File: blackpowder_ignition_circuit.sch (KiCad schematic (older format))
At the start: 11 parts, among them J2 Conn_01x02, J3 Conn_01x02, Q1 FDS6898A, Q2 Q_DUAL_PMOS_S1G1D2S2G2D1, U2 TC4427AVOA

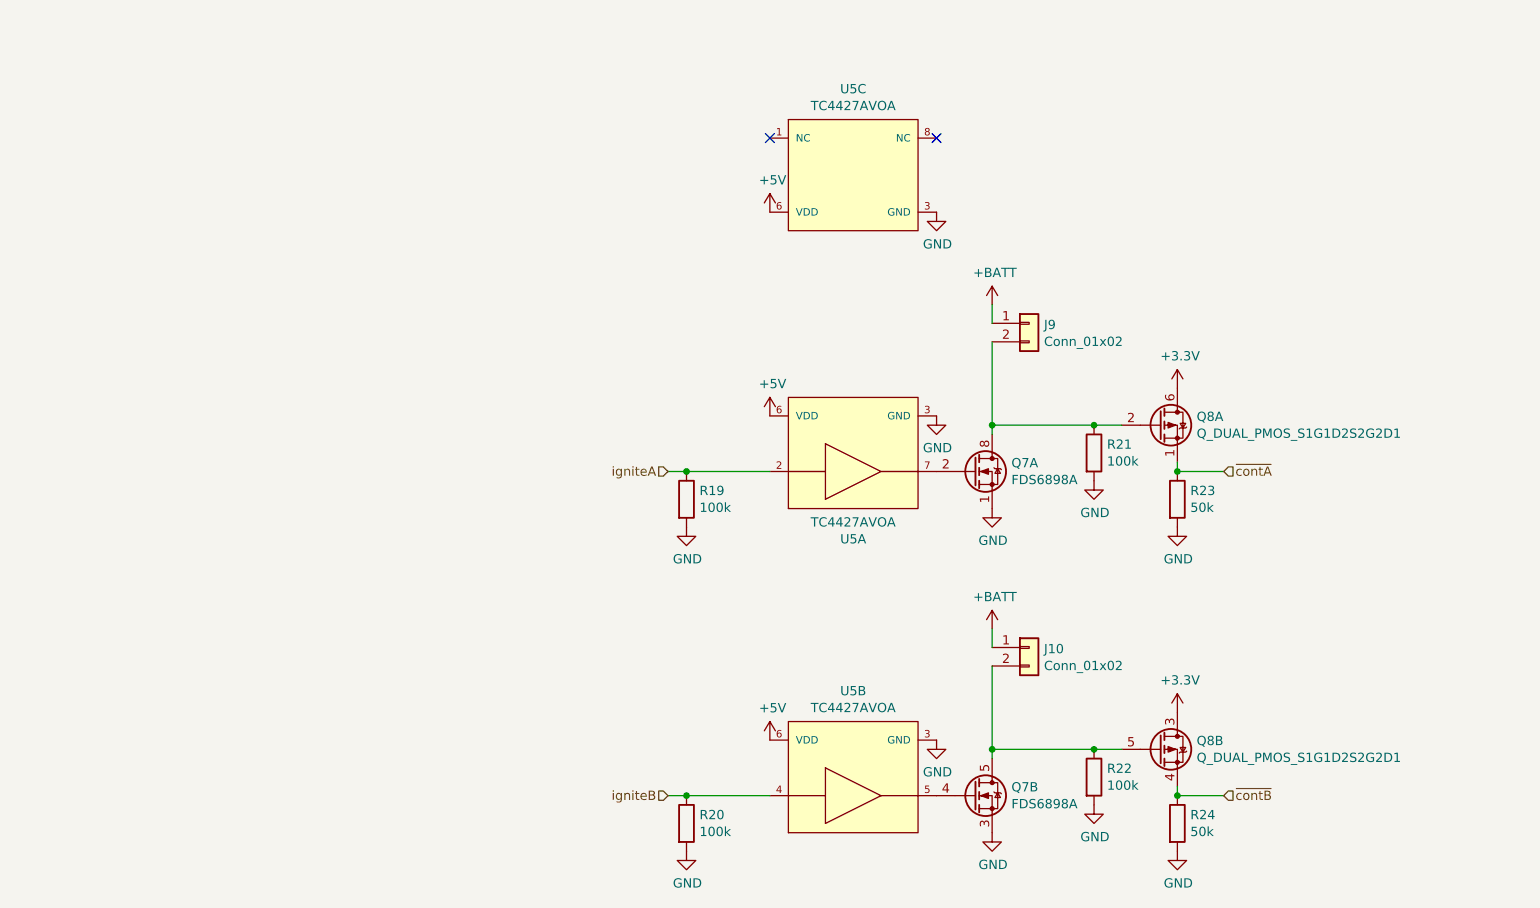
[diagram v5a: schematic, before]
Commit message: added digikey and manf part numbers, BAC logo
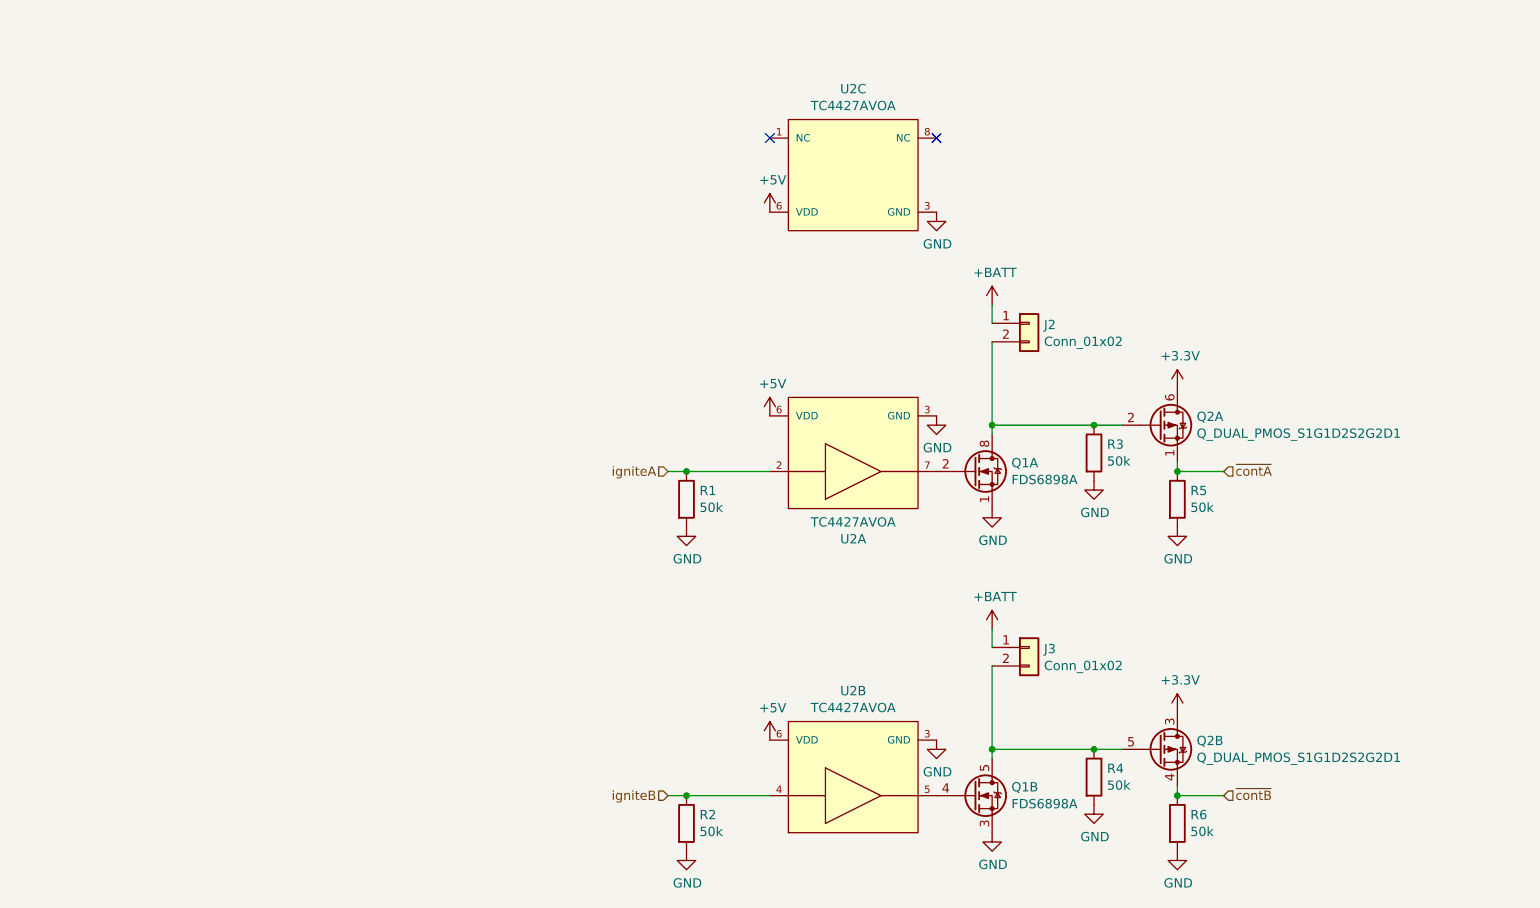
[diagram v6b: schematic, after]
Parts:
- removed R4: 50k, Resistor_SMD:R_0603_1608Metric_Pad0.98x0.95mm_HandSolder, symbol Device:R
- removed R4: 100k, Resistor_SMD:R_0603_1608Metric_Pad0.98x0.95mm_HandSolder, symbol Device:R
- added R4, R5: 50k, Resistor_SMD:R_0603_1608Metric_Pad0.98x0.95mm_HandSolder, symbol Device:R
- J2, J3: DIGIKEY (none) -> WM16206-ND; MANF (none) -> 1724480002
- Q1: DIGIKEY (none) -> FDS6898ACT-ND; MANF (none) -> FDS6898A
- Q2: DIGIKEY (none) -> 742-SI1967DH-T1-BE3CT-ND; MANF (none) -> SI1967DH-T1-BE3
- R1, R2, R3: value 100k -> 50k; DIGIKEY (none) -> 311-51KGRCT-ND; MANF (none) -> RC0603JR-0751KL
- R6: DIGIKEY (none) -> 311-51KGRCT-ND; MANF (none) -> RC0603JR-0751KL
- U2: DIGIKEY (none) -> TC4427AVOA-ND; MANF (none) -> TC4427AVOA
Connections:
- net GND: now also R4.2, R5.2
- net ~contA~: now also R5.1
- net at J3.2 (Pin_2), Q1.5 (D2), Q1.6 (D2)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: now also R4.1

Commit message: updates based on review
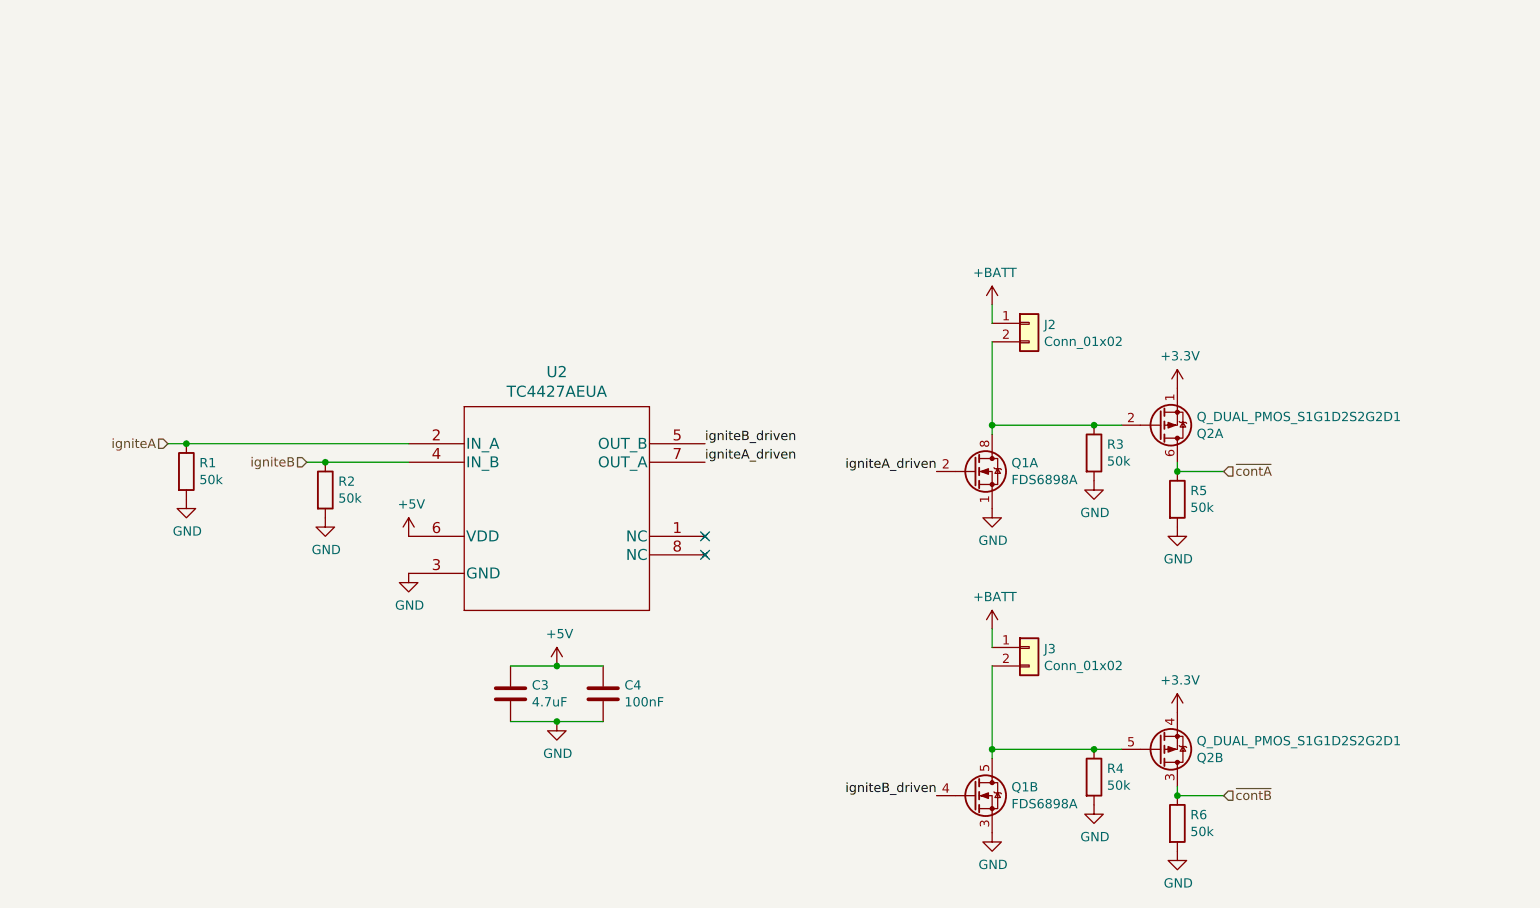
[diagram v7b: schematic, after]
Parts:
- removed U2: TC4427AVOA, Package_SO:MSOP-8-1EP_3x3mm_P0.65mm_EP2.5x3mm_Mask1.73x2.36mm, symbol eec:TC4427AVOA
- added C5: 4.7uF, Capacitor_SMD:C_0603_1608Metric_Pad1.08x0.95mm_HandSolder, symbol Device:C
- added C6: 100nF, Capacitor_SMD:C_0603_1608Metric_Pad1.08x0.95mm_HandSolder, symbol Device:C
- added U2: TC4427AEUA, star-common-lib:TC4427AEUA, symbol star-common-lib:TC4427AEUA
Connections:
- net +3V3: now also Q2.1 (S), Q2.4 (S); no longer Q2.3 (D), Q2.6 (D)
- net +5V: now also C5.1, C6.1, U2.6 (VDD)
- net GND: now also C5.2, C6.2, U2.3 (GND)
- net igniteA: now also U2.2 (IN_A)
- net igniteB: now also U2.4 (IN_B)
- net ~contA~: now also Q2.6 (D); no longer Q2.1 (S)
- net ~contB~: now also Q2.3 (D); no longer Q2.4 (S)
- net igniteA_driven: now reaches Q1.2 (G1)
- net igniteA_driven: now also U2.7 (OUT_A)
- net igniteB_driven: now reaches Q1.4 (G2)
- net igniteB_driven: now also U2.5 (OUT_B)
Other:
- moved on the sheet: R1, R2

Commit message: added diodes for esd
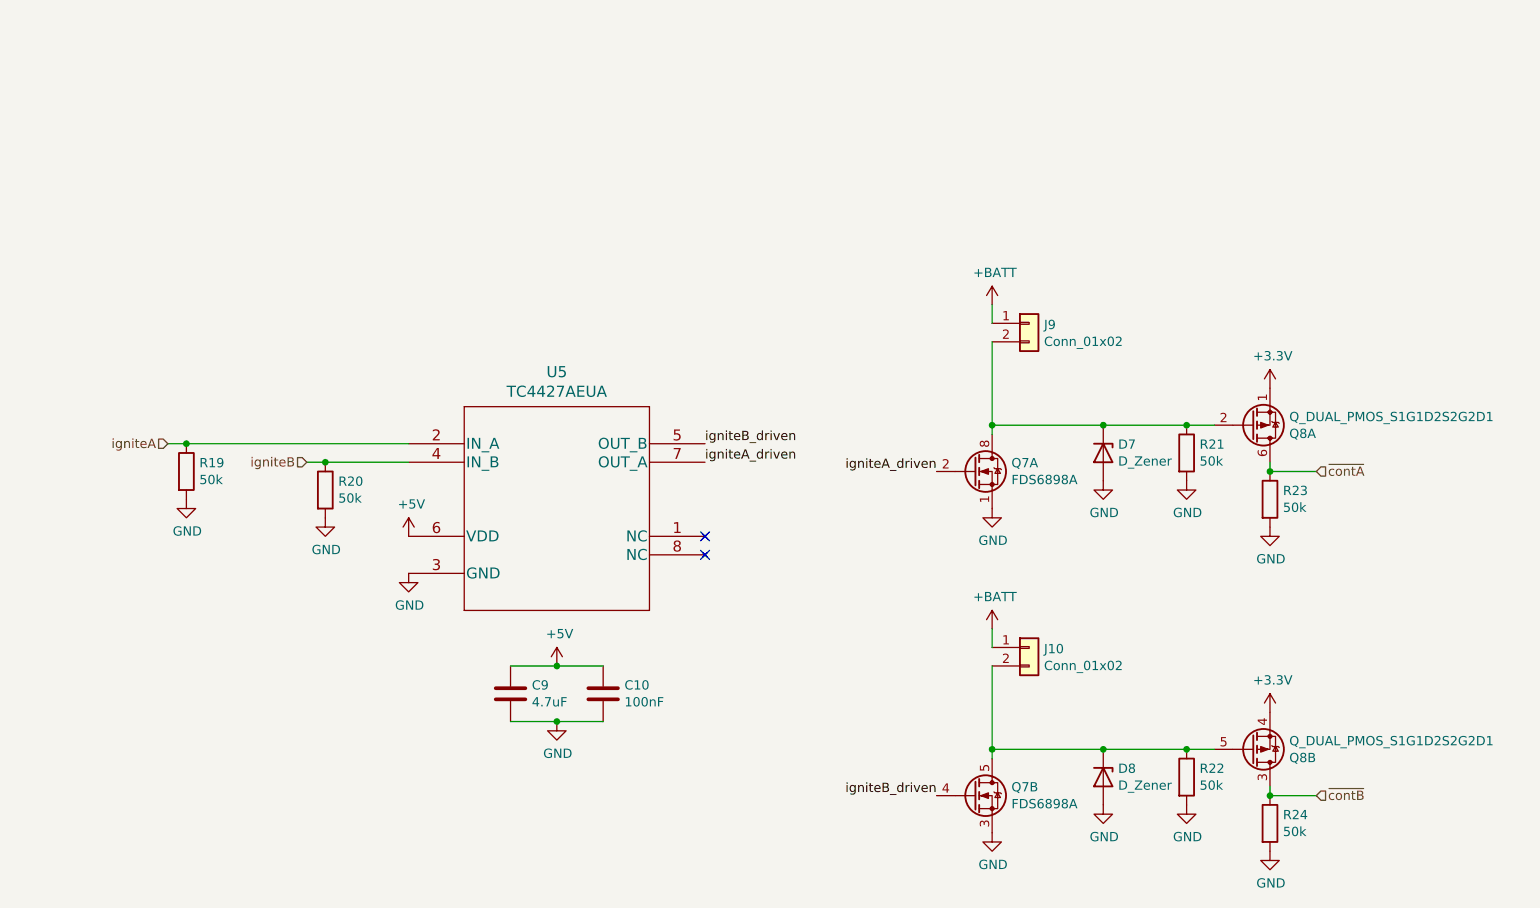
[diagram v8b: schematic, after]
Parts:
- added D1, D2: D_Zener, Diode_SMD:D_0603_1608Metric_Pad1.05x0.95mm_HandSolder, symbol Device:D_Zener
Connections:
- net GND: now also D1.2 (A), D2.2 (A)
- net at J2.2 (Pin_2), Q1.7 (D1), Q1.8 (D1)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: now also D1.1 (K)
- net at J3.2 (Pin_2), Q1.5 (D2), Q1.6 (D2)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: now also D2.1 (K)
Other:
- moved on the sheet: Q8A, Q8B, R21, R22, R23, R24
